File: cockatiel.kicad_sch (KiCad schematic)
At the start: 47 parts, among them J1 Programmer, J10 LED1_EXT, J11 LED1_SEL, J12 LED0_EXT, J13 LED0_SEL, J14 I/O Debug, J15 MIC_P_BYPASS, J16 MIC_N_BYPASS, J17 MIC_P_SEL, J18 MIC_N_SEL, J19 Cox Box Mic In, J2 USB, J20 Cox Box Mic Out, J21 Microphone out, J22 Headset Socket, J3 DEBUG_UART, J4 RESET, J5 Magnetic connector, J6 PANEL_POWER_BUTTON (MFB), J7 Battery Connector, J8 LED2_EXT, J9 LED2_SEL, T1 Transformer_Audio, U1 F-3188_CSR8645

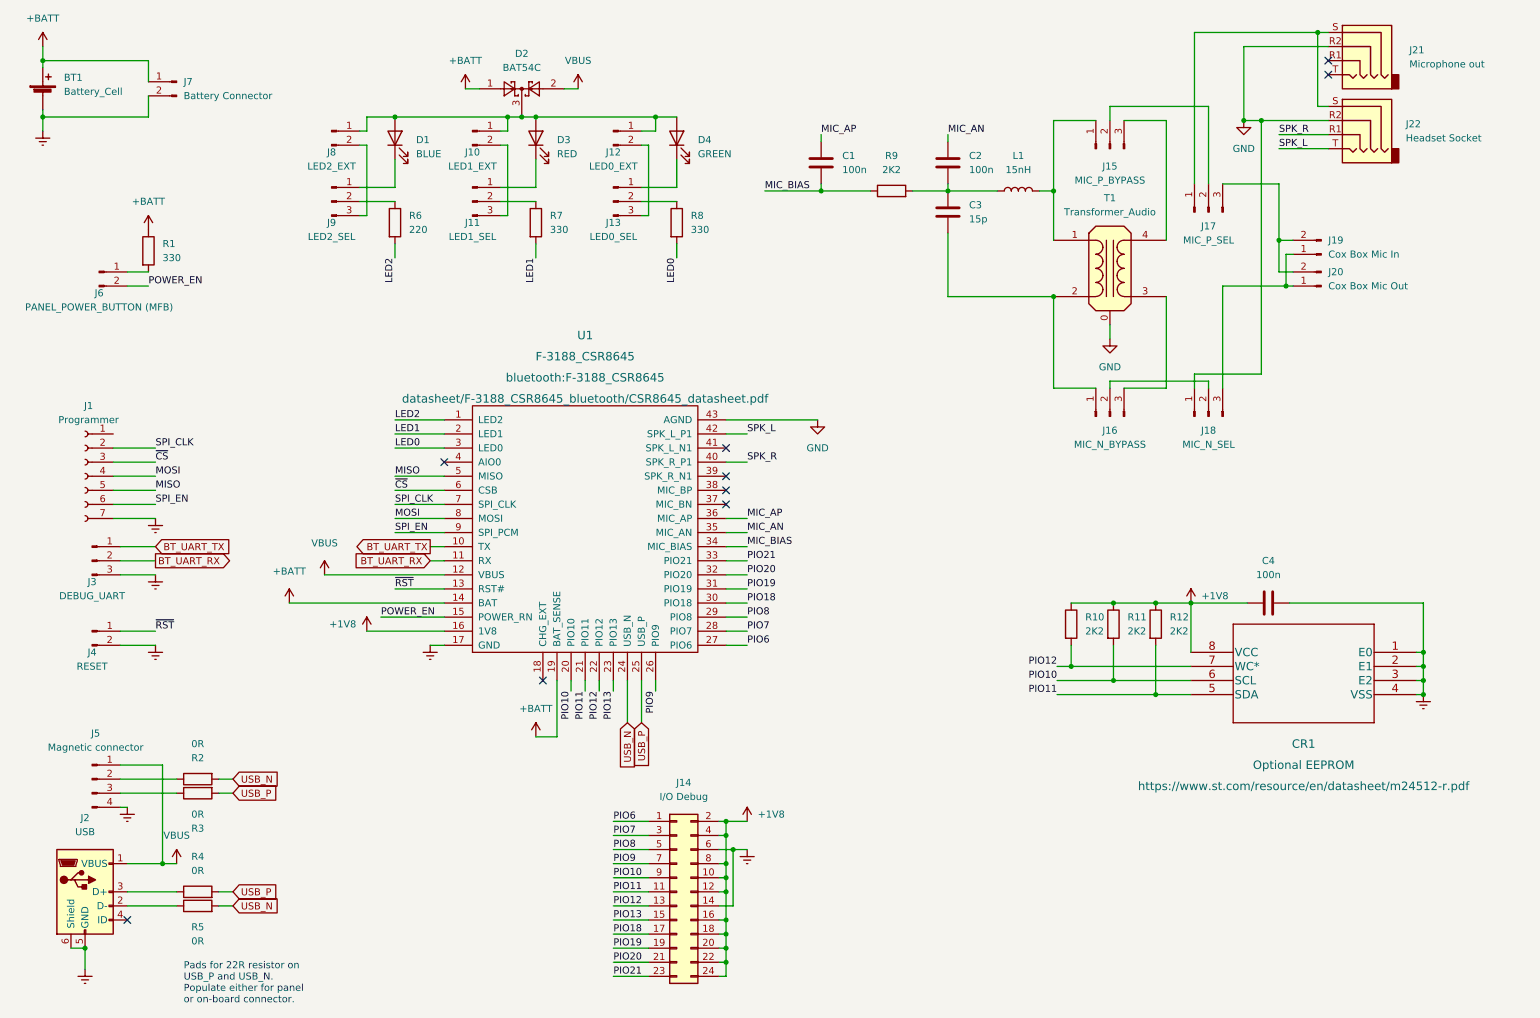
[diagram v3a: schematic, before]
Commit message: WIP
1. Add transformer footprint.
2. PCB routing
3. Misc changes to re-add JLCPCB part numbers.
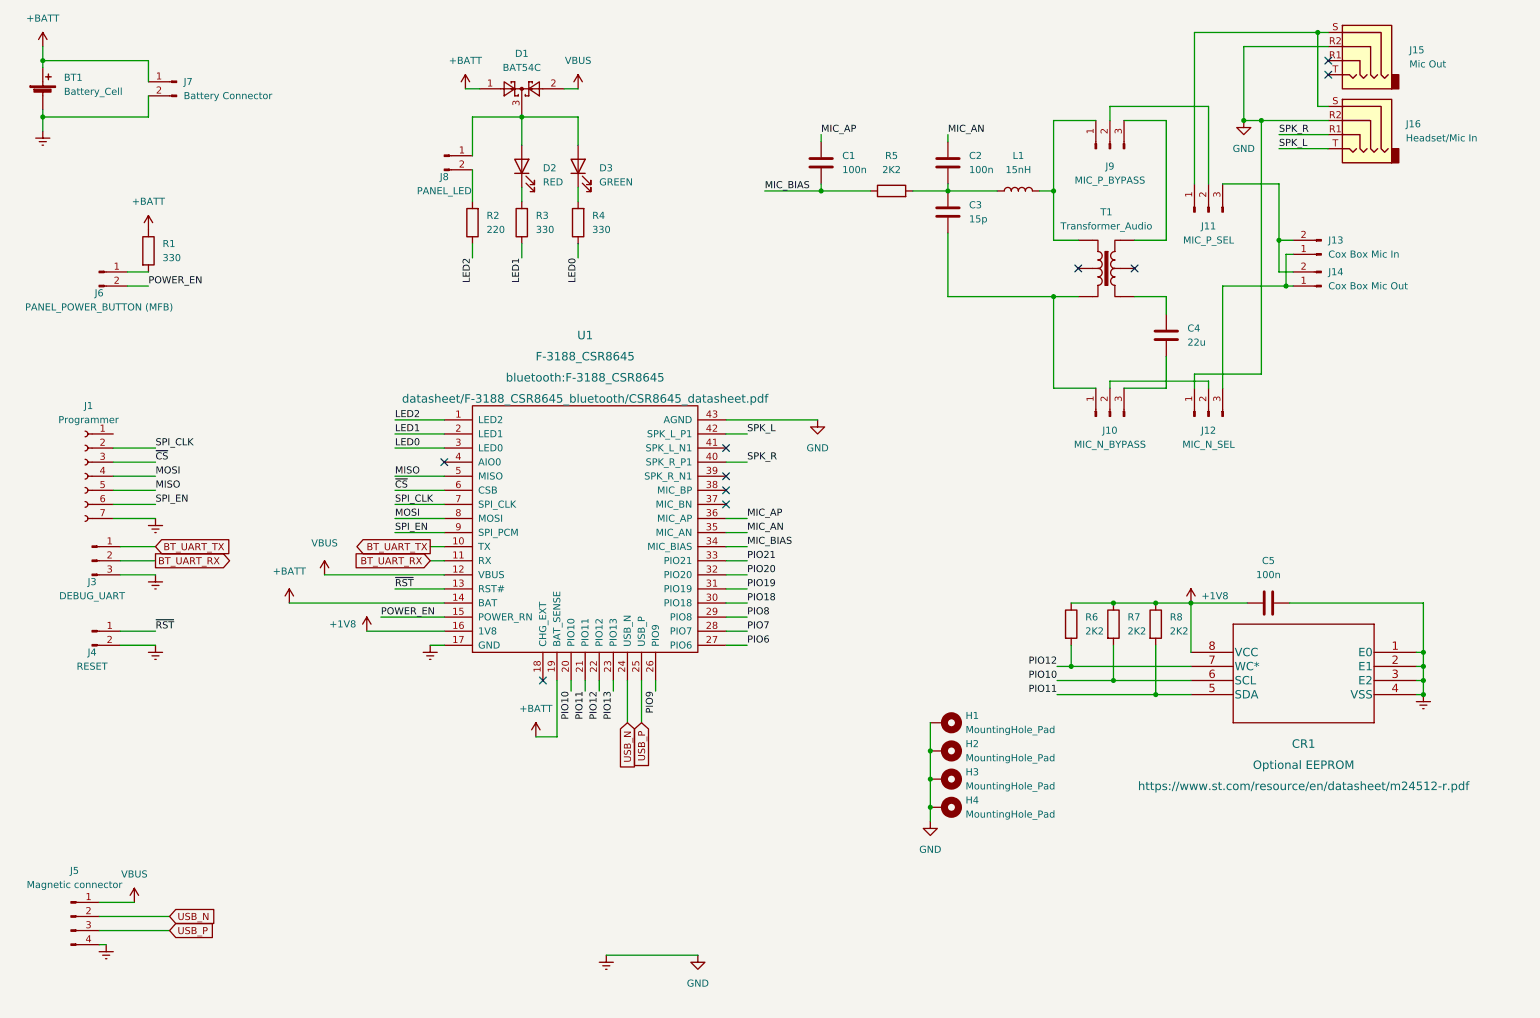
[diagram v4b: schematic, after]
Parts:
- removed D1: BLUE, LED_SMD:LED_0805_2012Metric_Pad1.15x1.40mm_HandSolder, symbol Device:LED
- removed J10: LED1_EXT, Connector_PinHeader_2.54mm:PinHeader_1x02_P2.54mm_Vertical, symbol Connector:Conn_01x02_Male
- removed J11: LED1_SEL, Connector_PinHeader_2.54mm:PinHeader_1x03_P2.54mm_Vertical, symbol Connector:Conn_01x03_Male
- removed J12: LED0_EXT, Connector_PinHeader_2.54mm:PinHeader_1x02_P2.54mm_Vertical, symbol Connector:Conn_01x02_Male
- removed J13: LED0_SEL, Connector_PinHeader_2.54mm:PinHeader_1x03_P2.54mm_Vertical, symbol Connector:Conn_01x03_Male
- removed J14: I/O Debug, Connector_PinHeader_2.54mm:PinHeader_2x07_P2.54mm_Vertical, symbol Connector_Generic:Conn_02x12_Odd_Even
- removed J2: USB, symbol Connector:USB_B_Micro
- removed J9: LED2_SEL, Connector_PinHeader_2.54mm:PinHeader_1x03_P2.54mm_Vertical, symbol Connector:Conn_01x03_Male
- removed R2, R3, R4, R5: 0R, Resistor_SMD:R_0805_2012Metric_Pad1.20x1.40mm_HandSolder, symbol Device:R
- added C4: 22u, Capacitor_SMD:C_1206_3216Metric_Pad1.33x1.80mm_HandSolder, symbol Device:C
- added H1, H2, H3, H4: MountingHole_Pad, MountingHole:MountingHole_3.2mm_M3_Pad_TopBottom, symbol Mechanical:MountingHole_Pad
- C1, C2: footprint (none) -> Capacitor_SMD:C_0805_2012Metric_Pad1.18x1.45mm_HandSolder; LCSC (none) -> C49678
- C3: footprint (none) -> Capacitor_SMD:C_0805_2012Metric_Pad1.18x1.45mm_HandSolder; LCSC (none) -> C107110
- C5: renamed from C4; LCSC (none) -> C49678
- D2: renamed from D3; footprint LED_SMD:LED_0805_2012Metric_Pad1.15x1.40mm_HandSolder -> LED_SMD:LED_0603_1608Metric_Pad1.05x0.95mm_HandSolder; LCSC (none) -> C2286
- D3: renamed from D4; footprint LED_SMD:LED_0805_2012Metric_Pad1.15x1.40mm_HandSolder -> LED_SMD:LED_0603_1608Metric_Pad1.05x0.95mm_HandSolder; LCSC (none) -> C72043
- J1: LCSC (none) -> C492406
- J15: renamed from J21; value Microphone out -> Mic Out; footprint Connector_Audio:Jack_3.5mm_CUI_SJ-3524-SMT_Horizontal -> Connector_Audio:Jack_3.5mm_PJ320D_Horizontal; LCSC (none) -> C521460
- J16: renamed from J22; value Headset Socket -> Headset/Mic In; footprint Connector_Audio:Jack_3.5mm_CUI_SJ-3524-SMT_Horizontal -> Connector_Audio:Jack_3.5mm_PJ320D_Horizontal; LCSC (none) -> C521460
- J4: LCSC C49257 -> C492401
- J5: LCSC (none) -> C225479
- J7: LCSC (none) -> C173752
- J8: value LED2_EXT -> PANEL_LED
- R1: LCSC (none) -> C17630
- R2: renamed from R6; LCSC (none) -> C17557
- R3: renamed from R7; LCSC (none) -> C17630
- R4: renamed from R8; LCSC (none) -> C17630
- R5: renamed from R9; LCSC (none) -> C17520
- R6: renamed from R10; footprint (none) -> Resistor_SMD:R_0805_2012Metric_Pad1.20x1.40mm_HandSolder; LCSC (none) -> C17520
- R7: renamed from R11; footprint (none) -> Resistor_SMD:R_0805_2012Metric_Pad1.20x1.40mm_HandSolder; LCSC (none) -> C17520
- R8: renamed from R12; footprint (none) -> Resistor_SMD:R_0805_2012Metric_Pad1.20x1.40mm_HandSolder; LCSC (none) -> C17520
- T1: footprint (none) -> cockateil:Transformer_Triad_T Y-141PN; symbol Device:Transformer_Audio -> Transformer:TRANSF5
- renumbered D2 to D1, J16 to J10, J17 to J11, J18 to J12, J19 to J13, J20 to J14, J15 to J9
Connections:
- net +1V8: now also C5.2; no longer C5.1
- net Earth: now also C5.1, J12.1 (Pin_1), J15.R2, J16.R2, U1.43 (AGND), H1.1, H2.1, H3.1, H4.1; no longer C5.2
- net LED0: now also R4.1; no longer R4.2
- net LED1: now also R3.1; no longer R3.2
- net LED2: now also R2.1; no longer R2.2
- net USB_N: now also J5.2 (Pin_2)
- net USB_P: now also J5.3 (Pin_3)
- net at C3.2, J10.1 (Pin_1): now also T1.4; no longer T1.2 (AB)
- net at J10.3 (Pin_3): now also C4.2; no longer T1.3 (SA)
- net at D2.1 (K): now also R3.2
- net at D3.1 (K): now also R4.2
- net at J8.2 (Pin_2): now also R2.2
- net at J9.1 (Pin_1), L1.2: now also T1.6; no longer T1.1 (AA)
- net at J9.3 (Pin_3): now also T1.1; no longer T1.4 (SB)
- removed net GND: J12.1 (Pin_1), J15.R2, J16.R2, T1.0, U1.43 (AGND)
- new net: C4.1, T1.3
- no-connect marks 9 -> 10
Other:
- note removed: "Pads for 22R resistor on USB_P and USB_N. Populate either for panel or on-board connector."
- moved on the sheet: C5, D2, D3, J5, R2, R3, R4

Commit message: Complete board layout and JLCPCB component allocation.
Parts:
- L1: LCSC (none) -> C27143
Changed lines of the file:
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@@
+      (effects (font (size 1.27 1.27)) hide)
+    )
+    (property "LCSC" "C27143" (id 4) (at 194.945 41.275 0)
       (effects (font (size 1.27 1.27)) hide)
     )

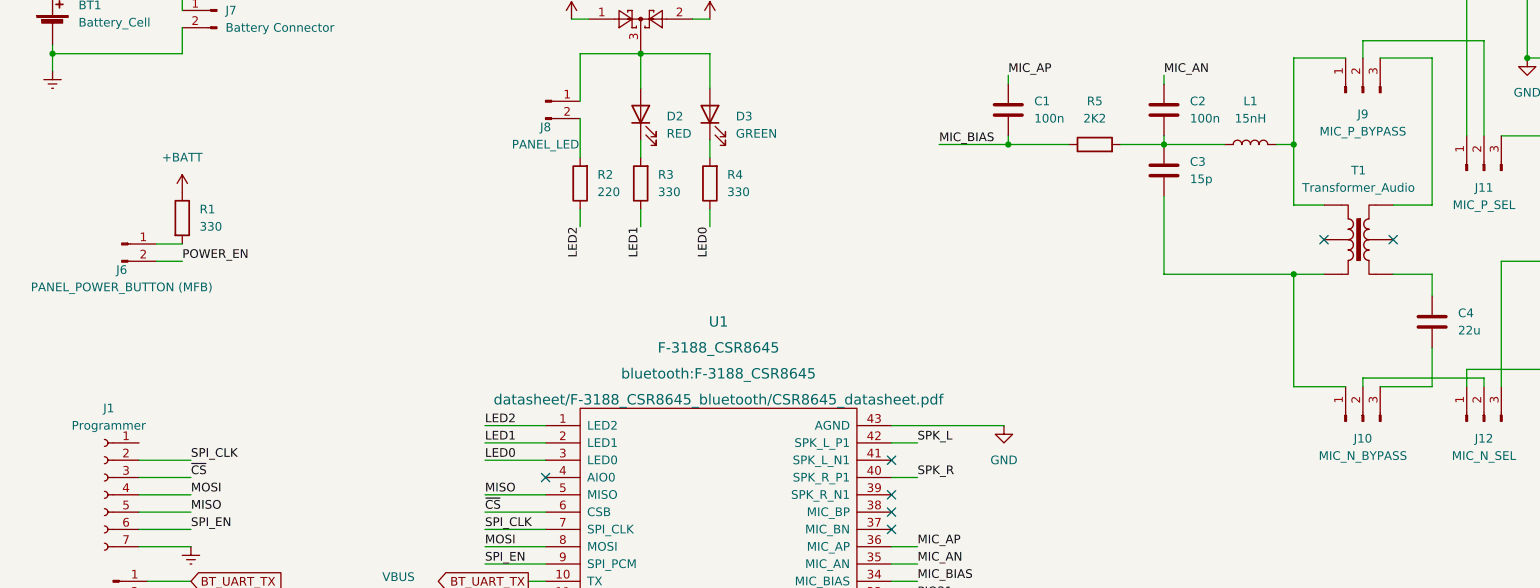
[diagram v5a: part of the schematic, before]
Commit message: Update part allocation
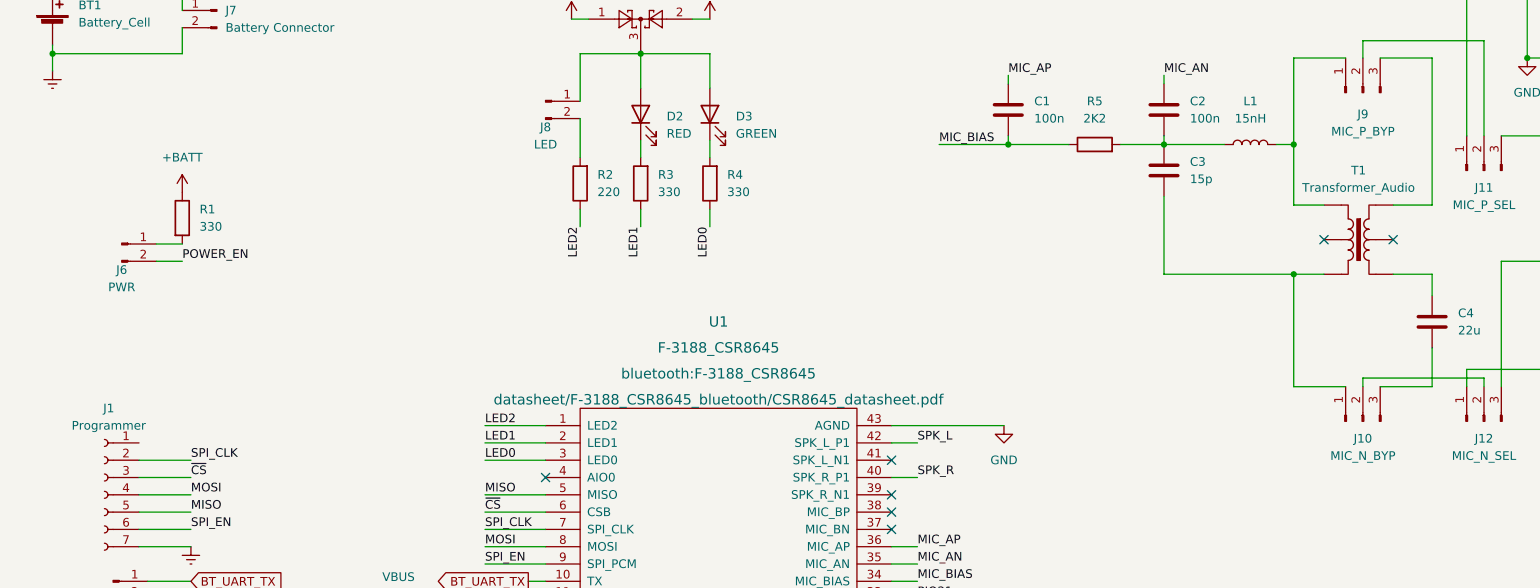
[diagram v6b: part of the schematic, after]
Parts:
- J10: value MIC_N_BYPASS -> MIC_N_BYP
- J6: value PANEL_POWER_BUTTON (MFB) -> PWR
- J8: value PANEL_LED -> LED
- J9: value MIC_P_BYPASS -> MIC_P_BYP
- L1: footprint Inductor_SMD:L_0805_2012Metric_Pad1.05x1.20mm_HandSolder -> Inductor_SMD:L_0402_1005Metric_Pad0.77x0.64mm_HandSolder
- T1: footprint cockateil:Transformer_Triad_T Y-141PN -> cockatiel:Transformer_Triad_T Y-141PN
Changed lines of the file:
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@@
     (in_bom yes) (on_board yes) (fields_autoplaced)
     (property "Reference" "J10" (id 0) (at 211.455 90.805 90))
-    (property "Value" "MIC_N_BYPASS" (id 1) (at 211.455 93.345 90))
+    (property "Value" "MIC_N_BYP" (id 1) (at 211.455 93.345 90))
     (property "Footprint" "Connector_PinHeader_2.54mm:PinHeader_1x03_P2.54mm_Vertical" (id 2) (at 211.455 88.265 0)
       (effects (font (size 1.27 1.27)) hide)
@@
     (in_bom yes) (on_board yes)
     (property "Reference" "J8" (id 0) (at 91.44 45.085 0))
-    (property "Value" "PANEL_LED" (id 1) (at 91.44 47.625 0))
+    (property "Value" "LED" (id 1) (at 91.44 47.625 0))
     (property "Footprint" "Connector_PinHeader_2.54mm:PinHeader_1x02_P2.54mm_Vertical" (id 2) (at 91.44 41.275 0)
       (effects (font (size 1.27 1.27)) hide)
@@
     (in_bom yes) (on_board yes)
     (property "Reference" "J6" (id 0) (at 29.21 66.04 0))
-    (property "Value" "PANEL_POWER_BUTTON (MFB)" (id 1) (at 29.21 68.58 0))
+    (property "Value" "PWR" (id 1) (at 29.21 68.58 0))
     (property "Footprint" "Connector_PinHeader_2.54mm:PinHeader_1x02_P2.54mm_Vertical" (id 2) (at 29.21 62.23 0)
       (effects (font (size 1.27 1.27)) hide)
@@
     (property "Reference" "T1" (id 0) (at 210.82 51.435 0))
     (property "Value" "Transformer_Audio" (id 1) (at 210.82 53.975 0))
-    (property "Footprint" "cockateil:Transformer_Triad_T Y-141PN" (id 2) (at 210.82 61.595 0)
+    (property "Footprint" "cockatiel:Transformer_Triad_T Y-141PN" (id 2) (at 210.82 61.595 0)
       (effects (font (size 1.27 1.27)) hide)
     )
@@
     (property "Reference" "L1" (id 0) (at 194.945 41.275 90))
     (property "Value" "15nH" (id 1) (at 194.945 43.815 90))
-    (property "Footprint" "Inductor_SMD:L_0805_2012Metric_Pad1.05x1.20mm_HandSolder" (id 2) (at 194.945 47.625 0)
+    (property "Footprint" "Inductor_SMD:L_0402_1005Metric_Pad0.77x0.64mm_HandSolder" (id 2) (at 194.945 47.625 0)
       (effects (font (size 1.27 1.27)) hide)
     )
@@
     (in_bom yes) (on_board yes) (fields_autoplaced)
     (property "Reference" "J9" (id 0) (at 211.455 43.18 90))
-    (property "Value" "MIC_P_BYPASS" (id 1) (at 211.455 45.72 90))
+    (property "Value" "MIC_P_BYP" (id 1) (at 211.455 45.72 90))
     (property "Footprint" "Connector_PinHeader_2.54mm:PinHeader_1x03_P2.54mm_Vertical" (id 2) (at 211.455 40.005 0)
       (effects (font (size 1.27 1.27)) hide)
@@
     )
     (path "/597501d4-6d2d-4f6a-a175-9a258bb0b552"
-      (reference "J6") (unit 1) (value "PANEL_POWER_BUTTON (MFB)") (footprint "Connector_PinHeader_2.54mm:PinHeader_1x02_P2.54mm_Vertical")
+      (reference "J6") (unit 1) (value "PWR") (footprint "Connector_PinHeader_2.54mm:PinHeader_1x02_P2.54mm_Vertical")
     )
     (path "/bc1f933b-c0f8-46eb-b1aa-4dc1985ef959"
@@
     )
     (path "/2f019ab0-d6fb-4af8-8459-162264a4a1ff"
-      (reference "J8") (unit 1) (value "PANEL_LED") (footprint "Connector_PinHeader_2.54mm:PinHeader_1x02_P2.54mm_Vertical")
+      (reference "J8") (unit 1) (value "LED") (footprint "Connector_PinHeader_2.54mm:PinHeader_1x02_P2.54mm_Vertical")
     )
     (path "/eac70146-2642-43ab-b28e-ab957e7eabdf"
-      (reference "J9") (unit 1) (value "MIC_P_BYPASS") (footprint "Connector_PinHeader_2.54mm:PinHeader_1x03_P2.54mm_Vertical")
+      (reference "J9") (unit 1) (value "MIC_P_BYP") (footprint "Connector_PinHeader_2.54mm:PinHeader_1x03_P2.54mm_Vertical")
     )
     (path "/1de3cbbf-45ab-49f0-b67d-ce7bb5faeb84"
-      (reference "J10") (unit 1) (value "MIC_N_BYPASS") (footprint "Connector_PinHeader_2.54mm:PinHeader_1x03_P2.54mm_Vertical")
+      (reference "J10") (unit 1) (value "MIC_N_BYP") (footprint "Connector_PinHeader_2.54mm:PinHeader_1x03_P2.54mm_Vertical")
     )
     (path "/cbf058c9-f6e8-4d64-a6ce-55d23fcbb262"
@@
     )
     (path "/c37583e6-c604-4aaf-93a5-b66170709844"
-      (reference "L1") (unit 1) (value "15nH") (footprint "Inductor_SMD:L_0805_2012Metric_Pad1.05x1.20mm_HandSolder")
+      (reference "L1") (unit 1) (value "15nH") (footprint "Inductor_SMD:L_0402_1005Metric_Pad0.77x0.64mm_HandSolder")
     )
     (path "/a7b88367-e071-4dad-a025-676cba3104ed"
@@
     )
     (path "/5f62a08e-6be9-45e2-bf22-6de3b21ef883"
-      (reference "T1") (unit 1) (value "Transformer_Audio") (footprint "cockateil:Transformer_Triad_T Y-141PN")
+      (reference "T1") (unit 1) (value "Transformer_Audio") (footprint "cockatiel:Transformer_Triad_T Y-141PN")
     )
     (path "/cd8320ae-7922-4c4d-bb7a-8f1cd3b5f307"

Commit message: Replace out of stock component with suitable equivalent
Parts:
- J15, J16: LCSC C521460 -> C95562
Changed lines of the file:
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@@
       (effects (font (size 1.27 1.27)) hide)
     )
-    (property "LCSC" "C521460" (id 4) (at 264.795 35.5599 0)
+    (property "LCSC" "C95562" (id 4) (at 264.795 35.5599 0)
       (effects (font (size 1.27 1.27)) hide)
     )
@@
       (effects (font (size 1.27 1.27)) hide)
     )
-    (property "LCSC" "C521460" (id 4) (at 265.43 22.2249 0)
-      (effects (font (size 1.27 1.27)) hide)
-    )
+    (property "LCSC" "C95562" (id 4) (at 265.43 22.2249 0)
+      (effects (font (size 1.27 1.27)) hide)
+    )
